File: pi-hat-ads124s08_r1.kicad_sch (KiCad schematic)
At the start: 21 parts, among them J1 GPIO, J2 Conn_01x06, J3 Conn_01x06, J4 Conn_01x06, J5 Conn_01x06, J6 Conn_01x04, J7 Conn_01x02, U1 M24c64, U3 XC6206P332MR

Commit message: initial cut.
power and serial interface first cut complete...
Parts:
- removed J6: Conn_01x04, Connector_PinHeader_2.54mm:PinHeader_1x04_P2.54mm_Vertical, symbol Connector_Generic:Conn_01x04
- added J6: Conn_01x06, Connector_PinHeader_2.54mm:PinHeader_1x06_P2.54mm_Vertical, symbol Connector_Generic:Conn_01x06
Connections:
- net EXE1+: no longer D3.1 (K), J3.1 (Pin_1), J4.6 (Pin_6)
- net EXE1-: no longer D3.2 (A), J3.6 (Pin_6), J4.1 (Pin_1)
- net GPIO10/SPI0.MOSI: now also J6.2 (Pin_2)
- net GPIO11/SPI0.SCLK: now also J6.3 (Pin_3)
- net GPIO8/SPI0.CE0: now also J6.5 (Pin_5)
- net GPIO9/SPI0.MISO: now also J6.4 (Pin_4)
- new net EXE2+: D3.1 (K), J3.1 (Pin_1), J4.6 (Pin_6)
- new net EXE2-: D3.2 (A), J3.6 (Pin_6), J4.1 (Pin_1)
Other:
- sheet Analog ports: added ADC_START, EXC2+, EXC2-, EXT_CLK, SPI_CLK, SPI_CS, SPI_MISO, SPI_MOSI, ~{ADC_READY}, ~{ADC_RST}; removed DCLK, DOUT, D_RATE, EXT_CLK_IN
- note added: "(We'll never use it, but make it possible!)"
- note added: "To use without a Pi.. TODO: re-order as convenient, not important for most of this"
- note removed: "To use without a Pi.."
- title: HX711 Linux IIO Eval PiHAT -> ADS124S08 Linux IIO Eval PiHAT

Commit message: blocking out...
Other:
- sheet Analog ports: added EXC1+, EXC1-, IN1+, IN1-, SENSE1+, SENSE1-; removed EXC+, EXC-, IN+, IN-, SENSE+, SENSE-
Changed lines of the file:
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@@
-			)
-		)
-		(pin "EXC+" bidirectional
-			(at 259.08 40.64 0)
-			(effects
-				(font
-					(size 1.27 1.27)
-				)
-				(justify right)
-			)
-		)
-		(pin "EXC-" bidirectional
-			(at 259.08 43.18 0)
-			(effects
-				(font
-					(size 1.27 1.27)
-				)
-				(justify right)
-			)
-		)
-		(pin "IN+" input
-			(at 259.08 45.72 0)
-			(effects
-				(font
-					(size 1.27 1.27)
-				)
-				(justify right)
-			)
-		)
-		(pin "IN-" input
-			(at 259.08 48.26 0)
-			(effects
-				(font
-					(size 1.27 1.27)
-				)
-				(justify right)
-			)
-		)
-		(pin "SENSE+" input
-			(at 259.08 50.8 0)
-			(effects
-				(font
-					(size 1.27 1.27)
-				)
-				(justify right)
-			)
-		)
-		(pin "SENSE-" input
-			(at 259.08 53.34 0)
-			(effects
-				(font
-					(size 1.27 1.27)
-				)
-				(justify right)
 			)
 		)
@@
 			(effects
 				(font
+					(size 1.27 1.27)
+				)
+				(justify right)
+			)
+		)
+		(pin "EXC1+" bidirectional
+			(at 259.08 40.64 0)
+			(effects
+				(font
+					(size 1.27 1.27)
+				)
+				(justify right)
+			)
+		)
+		(pin "EXC1-" bidirectional
+			(at 259.08 43.18 0)
+			(effects
+				(font
+					(size 1.27 1.27)
+				)
+				(justify right)
+			)
+		)
+		(pin "IN1+" input
+			(at 259.08 45.72 0)
+			(effects
+				(font
+					(size 1.27 1.27)
+				)
+				(justify right)
+			)
+		)
+		(pin "IN1-" input
+			(at 259.08 48.26 0)
+			(effects
+				(font
+					(size 1.27 1.27)
+				)
+				(justify right)
+			)
+		)
+		(pin "SENSE1+" input
+			(at 259.08 50.8 0)
+			(effects
+				(font
+					(size 1.27 1.27)
+				)
+				(justify right)
+			)
+		)
+		(pin "SENSE1-" input
+			(at 259.08 53.34 0)
+			(effects
+				(font

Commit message: progressing, blocking things out, pondering orbz
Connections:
- net GPIO10/SPI0.MOSI: now also J6.4 (Pin_4); no longer J6.2 (Pin_2)
- net GPIO24: now also J6.1 (Pin_1)
- net GPIO5: now also J6.6 (Pin_6)
- net GPIO9/SPI0.MISO: now also J6.2 (Pin_2); no longer J6.4 (Pin_4)
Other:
- note added: "To use without a Pi.. Is start more important than reset? Use 2x 4 instead? can be routed without as much splatter?"
- note removed: "To use without a Pi.. TODO: re-order as convenient, not important for most of this"

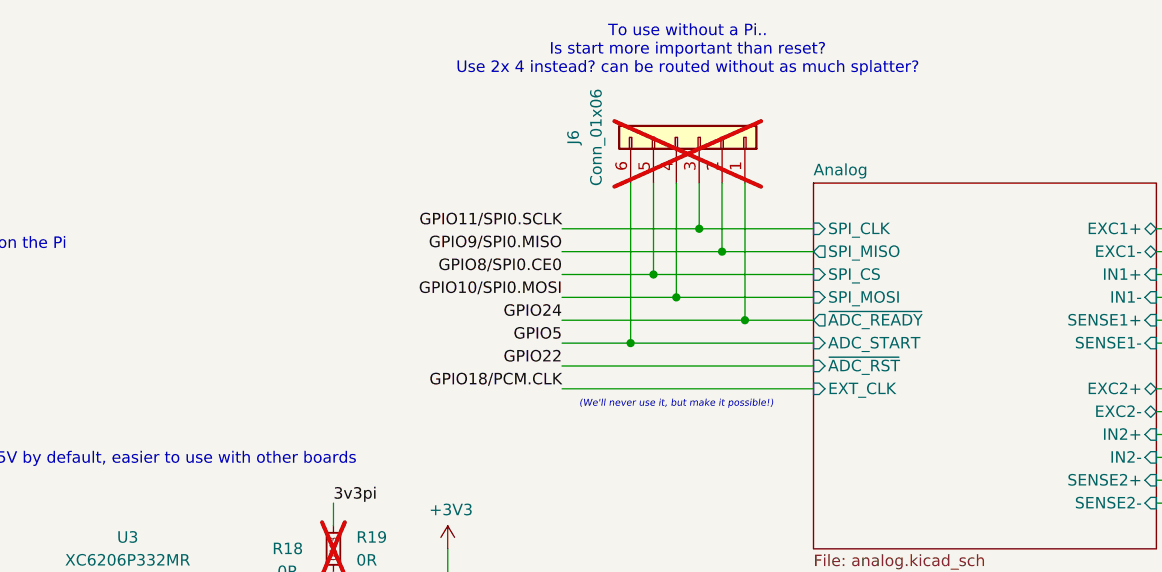
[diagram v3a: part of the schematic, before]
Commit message: notes and tweaks.
notes on inputs, filter ref, spi series R.
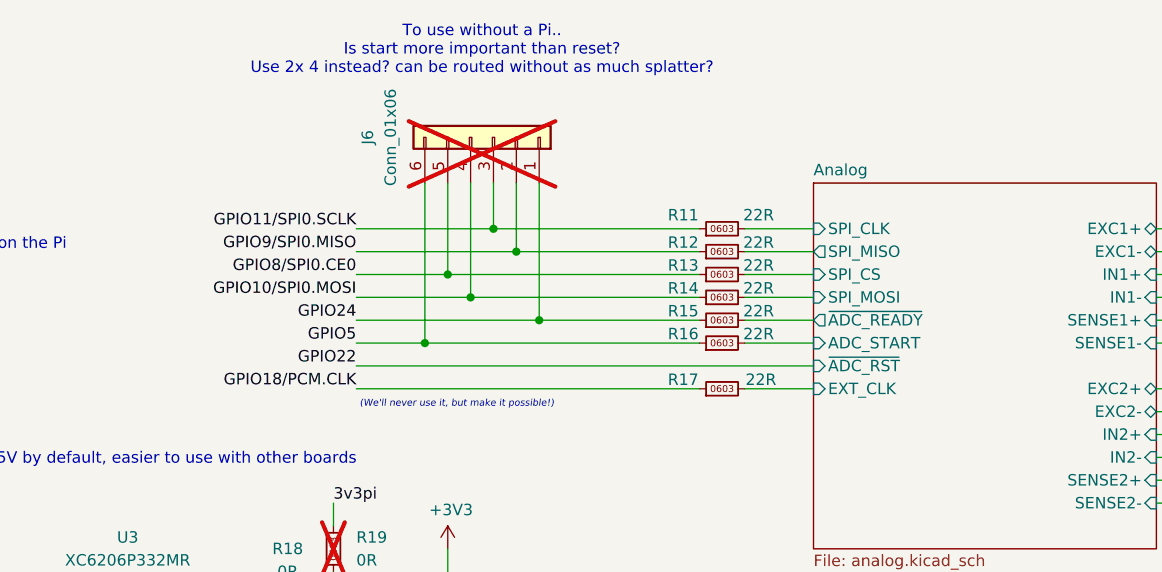
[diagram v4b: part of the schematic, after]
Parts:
- added R11, R12, R13, R14, R15, R16, R17: 22R, Resistor_SMD:R_0603_1608Metric, symbol karl-atomic-basic:KR0603_22R
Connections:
- net GPIO10/SPI0.MOSI: now also R14.1
- net GPIO11/SPI0.SCLK: now also R11.1
- net GPIO18/PCM.CLK: now also R17.1
- net GPIO24: now also R15.1
- net GPIO5: now also R16.1
- net GPIO8/SPI0.CE0: now also R13.1
- net GPIO9/SPI0.MISO: now also R12.1
- new net Analog/ADC_START: R16.2
- new net Analog/EXT_CLK: R17.2
- new net Analog/SPI_CLK: R11.2
- new net Analog/SPI_CS: R13.2
- new net Analog/SPI_MISO: R12.2
- new net Analog/SPI_MOSI: R14.2
- new net Analog/~{ADC_READY}: R15.2
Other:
- moved on the sheet: J6

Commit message: overhausl inputs a lot
read too much, thought too much.
try one with the "just 0R plus a nice big good quality cap" from the TI
precision seminar, describing common realities, as well as mixing in
what they did on the ads1262ref scale design document for the second
channel with a more "full blown" input filter.

I don't really like how none of this seems to be a proper AA filter,
but... ok.
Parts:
- C1: symbol karl-marel-atomics:KC0603_100nF -> karl-atomic-basic:KC0603_100nF
- C15, C16: symbol karl-marel-atomics:KC0603_1uF -> karl-atomic-basic:KC0603_1uF
- D2, D3: symbol karl-marel-atomics:SMF5.0A -> karl-atomic-basic:SMF5.0A
- R1, R3: symbol karl-marel-atomics:KR0603_3k9 -> karl-atomic-basic:KR0603_3k9
- R11, R12, R13, R14, R15, R16, R17: jlcbasic (none) -> basic
- R18, R19: symbol karl-marel-atomics:KR0603_0R -> karl-atomic-basic:KR0603_0R
- X1: symbol karl-marel-atomics:SYM_LABEL -> karl-atomic-basic:SYM_LABEL
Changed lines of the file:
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@@
 	)
 	(symbol
-		(lib_id "karl-marel-atomics:SYM_LABEL")
+		(lib_id "karl-atomic-basic:SYM_LABEL")
 		(at 147.32 181.61 0)
 		(unit 1)
@@
 	)
 	(symbol
-		(lib_id "karl-marel-atomics:KC0603_100nF")
+		(lib_id "karl-atomic-basic:KC0603_100nF")
 		(at 66.04 177.8 0)
 		(unit 1)
@@
 	)
 	(symbol
-		(lib_id "karl-marel-atomics:KR0603_0R")
+		(lib_id "karl-atomic-basic:KR0603_0R")
 		(at 167.64 76.2 180)
 		(unit 1)
@@
 	)
 	(symbol
-		(lib_id "karl-marel-atomics:SMF5.0A")
+		(lib_id "karl-atomic-basic:SMF5.0A")
 		(at 190.5 149.86 270)
 		(unit 1)
@@
 			)
 		)
+		(property "jlcbasic" "basic"
+			(at 210.82 43.18 0)
+			(effects
+				(font
+					(size 1.27 1.27)
+				)
+				(hide yes)
+			)
+		)
 		(pin "2"
 		)
@@
 	)
 	(symbol
-		(lib_id "karl-marel-atomics:KR0603_3k9")
+		(lib_id "karl-atomic-basic:KR0603_3k9")
 		(at 101.6 170.18 0)
 		(unit 1)
@@
 	)
 	(symbol
-		(lib_id "karl-marel-atomics:KC0603_1uF")
+		(lib_id "karl-atomic-basic:KC0603_1uF")
 		(at 127 86.36 0)
 		(unit 1)
@@
 			)
 		)
+		(property "jlcbasic" "basic"
+			(at 210.82 50.8 0)
+			(effects
+				(font
+					(size 1.27 1.27)
+				)
+				(hide yes)
+			)
+		)
 		(pin "2"
 		)
@@
 			)
 		)
+		(property "jlcbasic" "basic"
+			(at 210.82 58.42 0)
+			(effects
+				(font
+					(size 1.27 1.27)
+				)
+				(hide yes)
+			)
+		)
 		(pin "2"
 		)
@@
 		)
 		(property "LCSC Part #" "C23345"
+			(at 210.82 48.26 0)
+			(effects
+				(font
+					(size 1.27 1.27)
+				)
+				(hide yes)
+			)
+		)
+		(property "jlcbasic" "basic"
 			(at 210.82 48.26 0)
 			(effects
@@
 	)
 	(symbol
-		(lib_id "karl-marel-atomics:KC0603_1uF")
+		(lib_id "karl-atomic-basic:KC0603_1uF")
 		(at 157.48 86.36 0)
 		(unit 1)
@@
 	)
 	(symbol
-		(lib_id "karl-marel-atomics:KR0603_3k9")
+		(lib_id "karl-atomic-basic:KR0603_3k9")
 		(at 93.98 170.18 0)
 		(unit 1)
@@
 			)
 		)
+		(property "jlcbasic" "basic"
+			(at 210.82 53.34 0)
+			(effects
+				(font
+					(size 1.27 1.27)
+				)
+				(hide yes)
+			)
+		)
 		(pin "2"
 		)
@@
 	)
 	(symbol
-		(lib_id "karl-marel-atomics:KR0603_0R")
+		(lib_id "karl-atomic-basic:KR0603_0R")
 		(at 162.56 81.28 90)
 		(unit 1)
@@
 			)
 		)
+		(property "jlcbasic" "basic"
+			(at 210.82 40.64 0)
+			(effects
+				(font
+					(size 1.27 1.27)
+				)
+				(hide yes)
+			)
+		)
 		(pin "2"
 		)
@@
 	)
 	(symbol
-		(lib_id "karl-marel-atomics:SMF5.0A")
+		(lib_id "karl-atomic-basic:SMF5.0A")
 		(at 215.9 149.86 270)
 		(unit 1)
@@
 			(at 210.82 45.72 0)
 			(effects
+				(font
+					(size 1.27 1.27)
+				)
+				(hide yes)
+			)
+		)
+		(property "jlcbasic" "basic"
+			(at 210.82 45.72 0)
+			(effects

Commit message: thanks, I hate it.
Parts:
- removed J6: Conn_01x06, Connector_PinHeader_2.54mm:PinHeader_1x06_P2.54mm_Vertical, symbol Connector_Generic:Conn_01x06
- added J6: Conn_02x04_Odd_Even, Connector_PinHeader_2.54mm:PinHeader_2x04_P2.54mm_Vertical, symbol Connector_Generic:Conn_02x04_Odd_Even
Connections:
- net GPIO10/SPI0.MOSI: now also J6.6 (Pin_6)
- net GPIO11/SPI0.SCLK: now also J6.5 (Pin_5)
- net GPIO18/PCM.CLK: now also J6.1 (Pin_1)
- net GPIO22: now also J6.2 (Pin_2)
- net GPIO24: now also J6.3 (Pin_3)
- net GPIO5: now also J6.8 (Pin_8)
- net GPIO8/SPI0.CE0: now also J6.7 (Pin_7)
- net GPIO9/SPI0.MISO: now also J6.4 (Pin_4)

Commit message: moarh updates
we commit to save our progress
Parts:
- JP1: footprint Jumper:SolderJumper-2_P1.3mm_Open_TrianglePad1.0x1.5mm -> jlc-extras:SolderJumper-2_P1.3mm_Open_TrianglePad0.9x1.8mm
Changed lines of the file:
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@@
 			)
 		)
-		(property "Footprint" "Jumper:SolderJumper-2_P1.3mm_Open_TrianglePad1.0x1.5mm"
+		(property "Footprint" "jlc-extras:SolderJumper-2_P1.3mm_Open_TrianglePad0.9x1.8mm"
 			(at 97.79 180.34 0)
 			(effects
